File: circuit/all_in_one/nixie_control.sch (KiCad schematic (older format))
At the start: 19 parts

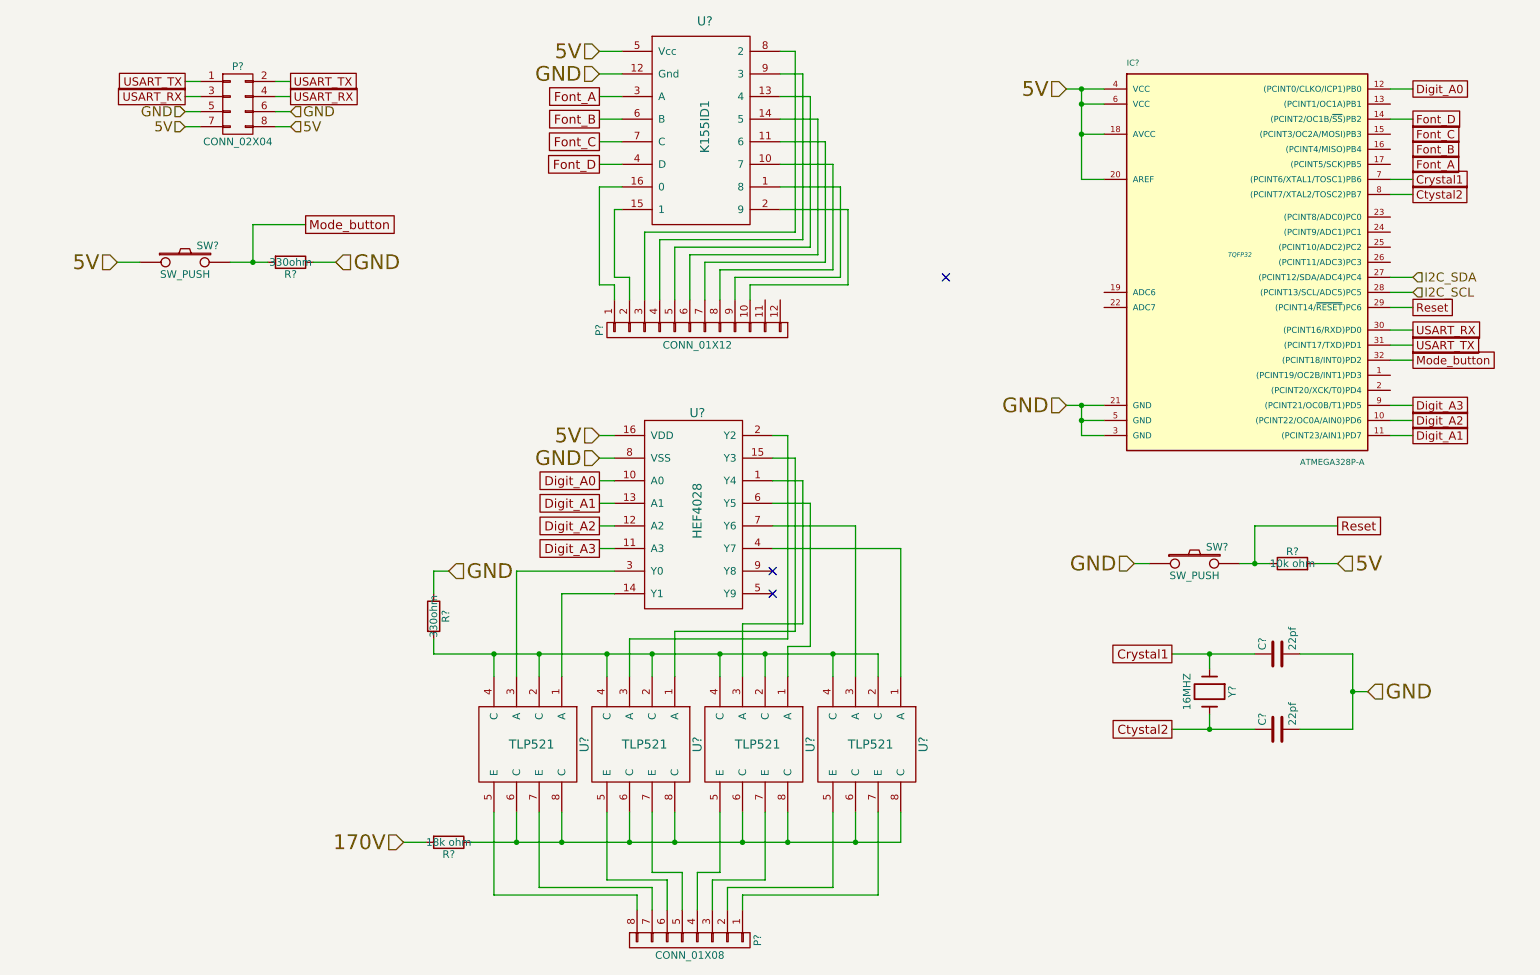
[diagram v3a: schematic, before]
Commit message: [All in one]Define part of compoment's footprint
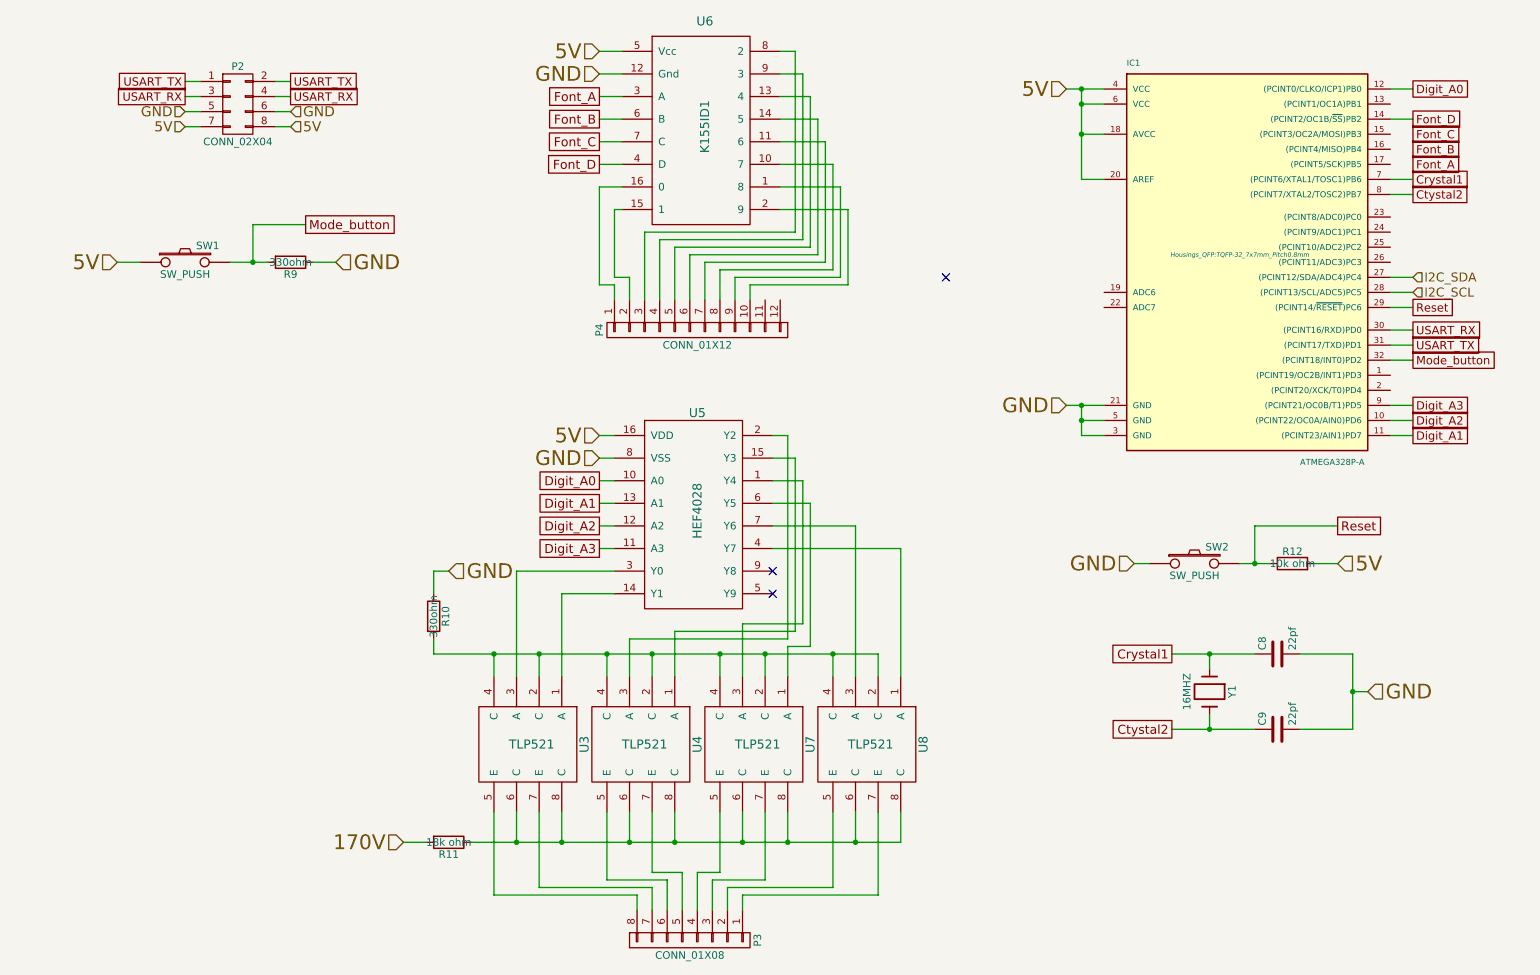
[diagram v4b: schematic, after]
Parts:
- IC1: renamed from IC?; footprint TQFP32 -> Housings_QFP:TQFP-32_7x7mm_Pitch0.8mm
- U3, U4, U7, U8: renamed from U?; footprint (none) -> SMD_Packages:DIP-8_SMD
- U5: renamed from U?; footprint (none) -> SMD_Packages:SO-16-N
- U6: renamed from U?; footprint (none) -> Housings_DIP:DIP-16_W7.62mm
- Y1: renamed from Y?; footprint (none) -> Crystals:Crystal_HC49-U_Vertical
- gave numbers to parts that had none: 11
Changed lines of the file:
@@
 GND
 $Comp
-L ATMEGA328P-A IC?
+L ATMEGA328P-A IC1
 U 1 1 5646C06F
 P 8850 2550
-F 0 "IC?" H 8100 3800 40  0000 L BNN
+F 0 "IC1" H 8100 3800 40  0000 L BNN
 F 1 "ATMEGA328P-A" H 9250 1150 40  0000 L BNN
-F 2 "TQFP32" H 8850 2550 30  0000 C CIN
+F 2 "Housings_QFP:TQFP-32_7x7mm_Pitch0.8mm" H 8850 2550 30  0000 C CIN
 F 3 "" H 8850 2550 60  0000 C CNN
 	1    8850 2550
@@
 5V
 $Comp
-L R R?
+L R R12
 U 1 1 5646C2E9
 P 9200 4600
-F 0 "R?" V 9280 4600 50  0000 C CNN
+F 0 "R12" V 9280 4600 50  0000 C CNN
 F 1 "10k ohm" V 9200 4600 50  0000 C CNN
-F 2 "" V 9130 4600 30  0000 C CNN
+F 2 "" V 9130 4600 30  0001 C CNN
 F 3 "" H 9200 4600 30  0000 C CNN
 	1    9200 4600
@@
 $EndComp
 $Comp
-L SW_PUSH SW?
+L SW_PUSH SW2
 U 1 1 5646C38C
 P 8550 4600
-F 0 "SW?" H 8700 4710 50  0000 C CNN
+F 0 "SW2" H 8700 4710 50  0000 C CNN
 F 1 "SW_PUSH" H 8550 4520 50  0000 C CNN
-F 2 "" H 8550 4600 60  0000 C CNN
+F 2 "" H 8550 4600 60  0001 C CNN
 F 3 "" H 8550 4600 60  0000 C CNN
 	1    8550 4600
@@
 Reset
 $Comp
-L C C?
+L C C8
 U 1 1 5646C6D0
 P 9100 5200
-F 0 "C?" H 9125 5300 50  0000 L CNN
+F 0 "C8" H 9125 5300 50  0000 L CNN
 F 1 "22pf" H 9125 5100 50  0000 L CNN
-F 2 "" H 9138 5050 30  0000 C CNN
+F 2 "" H 9138 5050 30  0001 C CNN
 F 3 "" H 9100 5200 60  0000 C CNN
 	1    9100 5200
@@
 $EndComp
 $Comp
-L C C?
+L C C9
 U 1 1 5646C741
 P 9100 5700
-F 0 "C?" H 9125 5800 50  0000 L CNN
+F 0 "C9" H 9125 5800 50  0000 L CNN
 F 1 "22pf" H 9125 5600 50  0000 L CNN
-F 2 "" H 9138 5550 30  0000 C CNN
+F 2 "" H 9138 5550 30  0001 C CNN
 F 3 "" H 9100 5700 60  0000 C CNN
 	1    9100 5700
@@
 $EndComp
 $Comp
-L Crystal Y?
+L Crystal Y1
 U 1 1 5646C7E1
 P 8650 5450
-F 0 "Y?" H 8650 5600 50  0000 C CNN
+F 0 "Y1" H 8650 5600 50  0000 C CNN
 F 1 "16MHZ" H 8650 5300 50  0000 C CNN
-F 2 "" H 8650 5450 60  0000 C CNN
+F 2 "Crystals:Crystal_HC49-U_Vertical" H 8650 5450 60  0001 C CNN
 F 3 "" H 8650 5450 60  0000 C CNN
 	1    8650 5450
@@
 Ctystal2
 $Comp
-L K155ID1 U?
+L K155ID1 U6
 U 1 1 5646D245
 P 5300 1750
-F 0 "U?" H 5300 2500 60  0000 C CNN
+F 0 "U6" H 5300 2500 60  0000 C CNN
 F 1 "K155ID1" V 5300 1800 60  0000 C CNN
-F 2 "" H 5300 2500 60  0000 C CNN
+F 2 "Housings_DIP:DIP-16_W7.62mm" H 5300 2500 60  0001 C CNN
 F 3 "" H 5300 2500 60  0000 C CNN
 	1    5300 1750
@@
 $EndComp
 $Comp
-L HEF4028 U?
+L HEF4028 U5
 U 1 1 5646D789
 P 5250 4300
-F 0 "U?" H 5250 5000 60  0000 C CNN
+F 0 "U5" H 5250 5000 60  0000 C CNN
 F 1 "HEF4028" V 5250 4350 60  0000 C CNN
-F 2 "" H 5250 5000 60  0000 C CNN
+F 2 "SMD_Packages:SO-16-N" H 5250 5000 60  0001 C CNN
 F 3 "" H 5250 5000 60  0000 C CNN
 	1    5250 4300
@@
 $EndComp
 $Comp
-L TLP521 U?
+L TLP521 U4
 U 1 1 5646D9AA
 P 4850 5800
-F 0 "U?" H 4850 6200 60  0000 C CNN
+F 0 "U4" H 4850 6200 60  0000 C CNN
 F 1 "TLP521" V 4850 5850 60  0000 C CNN
-F 2 "" H 4850 6200 60  0000 C CNN
+F 2 "SMD_Packages:DIP-8_SMD" H 4850 6200 60  0001 C CNN
 F 3 "" H 4850 6200 60  0000 C CNN
 	1    4850 5800
@@
 $EndComp
 $Comp
-L TLP521 U?
+L TLP521 U3
 U 1 1 5646DC40
 P 4100 5800
-F 0 "U?" H 4100 6200 60  0000 C CNN
+F 0 "U3" H 4100 6200 60  0000 C CNN
 F 1 "TLP521" V 4100 5850 60  0000 C CNN
-F 2 "" H 4100 6200 60  0000 C CNN
+F 2 "SMD_Packages:DIP-8_SMD" H 4100 6200 60  0001 C CNN
 F 3 "" H 4100 6200 60  0000 C CNN
 	1    4100 5800
@@
 $EndComp
 $Comp
-L TLP521 U?
+L TLP521 U8
 U 1 1 5646DD0A
 P 6350 5800
-F 0 "U?" H 6350 6200 60  0000 C CNN
+F 0 "U8" H 6350 6200 60  0000 C CNN
 F 1 "TLP521" V 6350 5850 60  0000 C CNN
-F 2 "" H 6350 6200 60  0000 C CNN
+F 2 "SMD_Packages:DIP-8_SMD" H 6350 6200 60  0001 C CNN
 F 3 "" H 6350 6200 60  0000 C CNN
 	1    6350 5800
@@
 $EndComp
 $Comp
-L TLP521 U?
+L TLP521 U7
 U 1 1 5646DD10
 P 5600 5800
-F 0 "U?" H 5600 6200 60  0000 C CNN
+F 0 "U7" H 5600 6200 60  0000 C CNN
 F 1 "TLP521" V 5600 5850 60  0000 C CNN
-F 2 "" H 5600 6200 60  0000 C CNN
+F 2 "SMD_Packages:DIP-8_SMD" H 5600 6200 60  0001 C CNN
 F 3 "" H 5600 6200 60  0000 C CNN
 	1    5600 5800
@@
 Digit_A3
 $Comp
-L R R?
+L R R11
 U 1 1 564700B5
 P 3600 6450
-F 0 "R?" V 3680 6450 50  0000 C CNN
+F 0 "R11" V 3680 6450 50  0000 C CNN
 F 1 "18k ohm" V 3600 6450 50  0000 C CNN
-F 2 "" V 3530 6450 30  0000 C CNN
+F 2 "" V 3530 6450 30  0001 C CNN
 F 3 "" H 3600 6450 30  0000 C CNN
 	1    3600 6450
@@
 $EndComp
 $Comp
-L CONN_01X08 P?
+L CONN_01X08 P3
 U 1 1 564704DB
 P 5200 7100
-F 0 "P?" H 5200 7550 50  0000 C CNN
+F 0 "P3" H 5200 7550 50  0000 C CNN
 F 1 "CONN_01X08" V 5300 7100 50  0000 C CNN
-F 2 "" H 5200 7100 60  0000 C CNN
+F 2 "" H 5200 7100 60  0001 C CNN
 F 3 "" H 5200 7100 60  0000 C CNN
 	1    5200 7100
@@
 Font_D
 $Comp
-L CONN_01X12 P?
+L CONN_01X12 P4
 U 1 1 56472490
 P 5250 3050
-F 0 "P?" H 5250 3700 50  0000 C CNN
+F 0 "P4" H 5250 3700 50  0000 C CNN
 F 1 "CONN_01X12" V 5350 3050 50  0000 C CNN
-F 2 "" H 5250 3050 60  0000 C CNN
+F 2 "" H 5250 3050 60  0001 C CNN
 F 3 "" H 5250 3050 60  0000 C CNN
 	1    5250 3050
@@
 	9850 3150 10000 3150
 $Comp
-L CONN_02X04 P?
+L CONN_02X04 P2
 U 1 1 56476352
 P 2200 1550
-F 0 "P?" H 2200 1800 50  0000 C CNN
+F 0 "P2" H 2200 1800 50  0000 C CNN
 F 1 "CONN_02X04" H 2200 1300 50  0000 C CNN
-F 2 "" H 2200 350 60  0000 C CNN
+F 2 "" H 2200 350 60  0001 C CNN
 F 3 "" H 2200 350 60  0000 C CNN
 	1    2200 1550
@@
 5V
 $Comp
-L SW_PUSH SW?
+L SW_PUSH SW1
 U 1 1 56478717
 P 1850 2600
-F 0 "SW?" H 2000 2710 50  0000 C CNN
+F 0 "SW1" H 2000 2710 50  0000 C CNN
 F 1 "SW_PUSH" H 1850 2520 50  0000 C CNN
-F 2 "" H 1850 2600 60  0000 C CNN
+F 2 "" H 1850 2600 60  0001 C CNN
 F 3 "" H 1850 2600 60  0000 C CNN
 	1    1850 2600
@@
 $EndComp
 $Comp
-L R R?
+L R R9
 U 1 1 5647877C
 P 2550 2600
-F 0 "R?" V 2630 2600 50  0000 C CNN
+F 0 "R9" V 2630 2600 50  0000 C CNN
 F 1 "330ohm" V 2550 2600 50  0000 C CNN
-F 2 "" V 2480 2600 30  0000 C CNN
+F 2 "" V 2480 2600 30  0001 C CNN
 F 3 "" H 2550 2600 30  0000 C CNN
 	1    2550 2600
@@
 NoConn ~ 6900 2700
 $Comp
-L R R?
+L R R10
 U 1 1 56483273
 P 3500 4950
-F 0 "R?" V 3580 4950 50  0000 C CNN
+F 0 "R10" V 3580 4950 50  0000 C CNN
 F 1 "330ohm" V 3500 4950 50  0000 C CNN
-F 2 "" V 3430 4950 30  0000 C CNN
+F 2 "" V 3430 4950 30  0001 C CNN
 F 3 "" H 3500 4950 30  0000 C CNN
 	1    3500 4950

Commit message: [All in one]Finish the tube display circuit
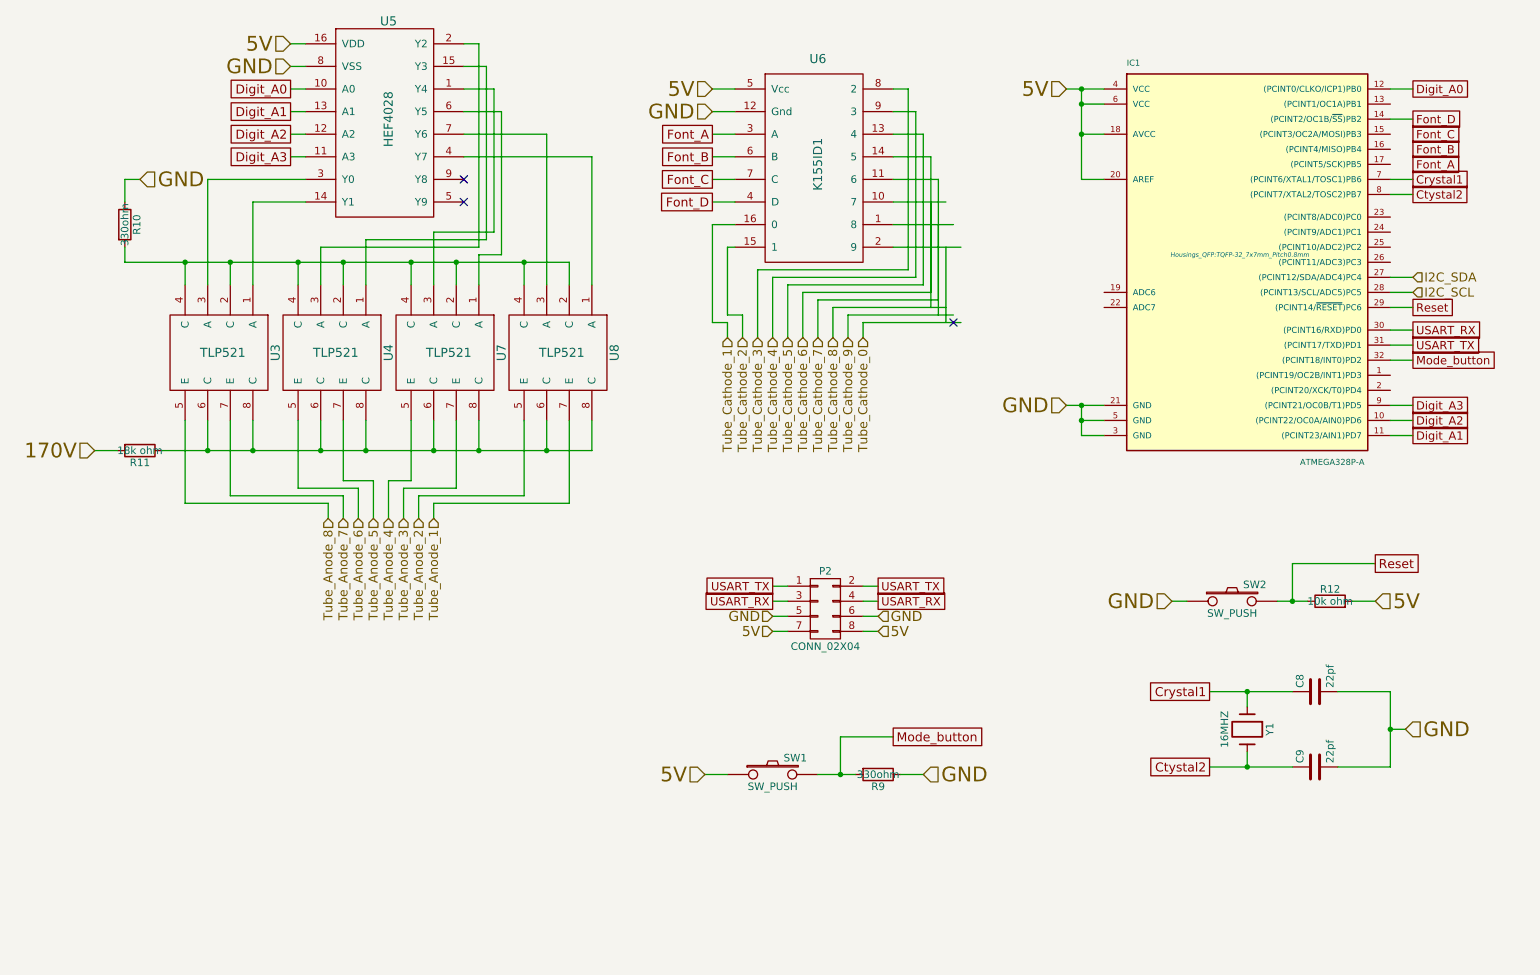
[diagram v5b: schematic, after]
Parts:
- removed P3: CONN_01X08, symbol CONN_01X08
- removed P4: CONN_01X12, symbol CONN_01X12
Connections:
- net labels added: Tube_Anode_1, Tube_Anode_2, Tube_Anode_3, Tube_Anode_4, Tube_Anode_5, Tube_Anode_6, Tube_Anode_7, Tube_Anode_8, Tube_Cathode_0, Tube_Cathode_1, Tube_Cathode_2, Tube_Cathode_3, Tube_Cathode_4, Tube_Cathode_5, Tube_Cathode_6, Tube_Cathode_7, Tube_Cathode_8, Tube_Cathode_9
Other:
- moved on the sheet: C8, C9, P2, R10, R11, R12, R9, SW1, SW2, U3, U4, U5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

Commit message: [All in one]Add tube comma control circuit
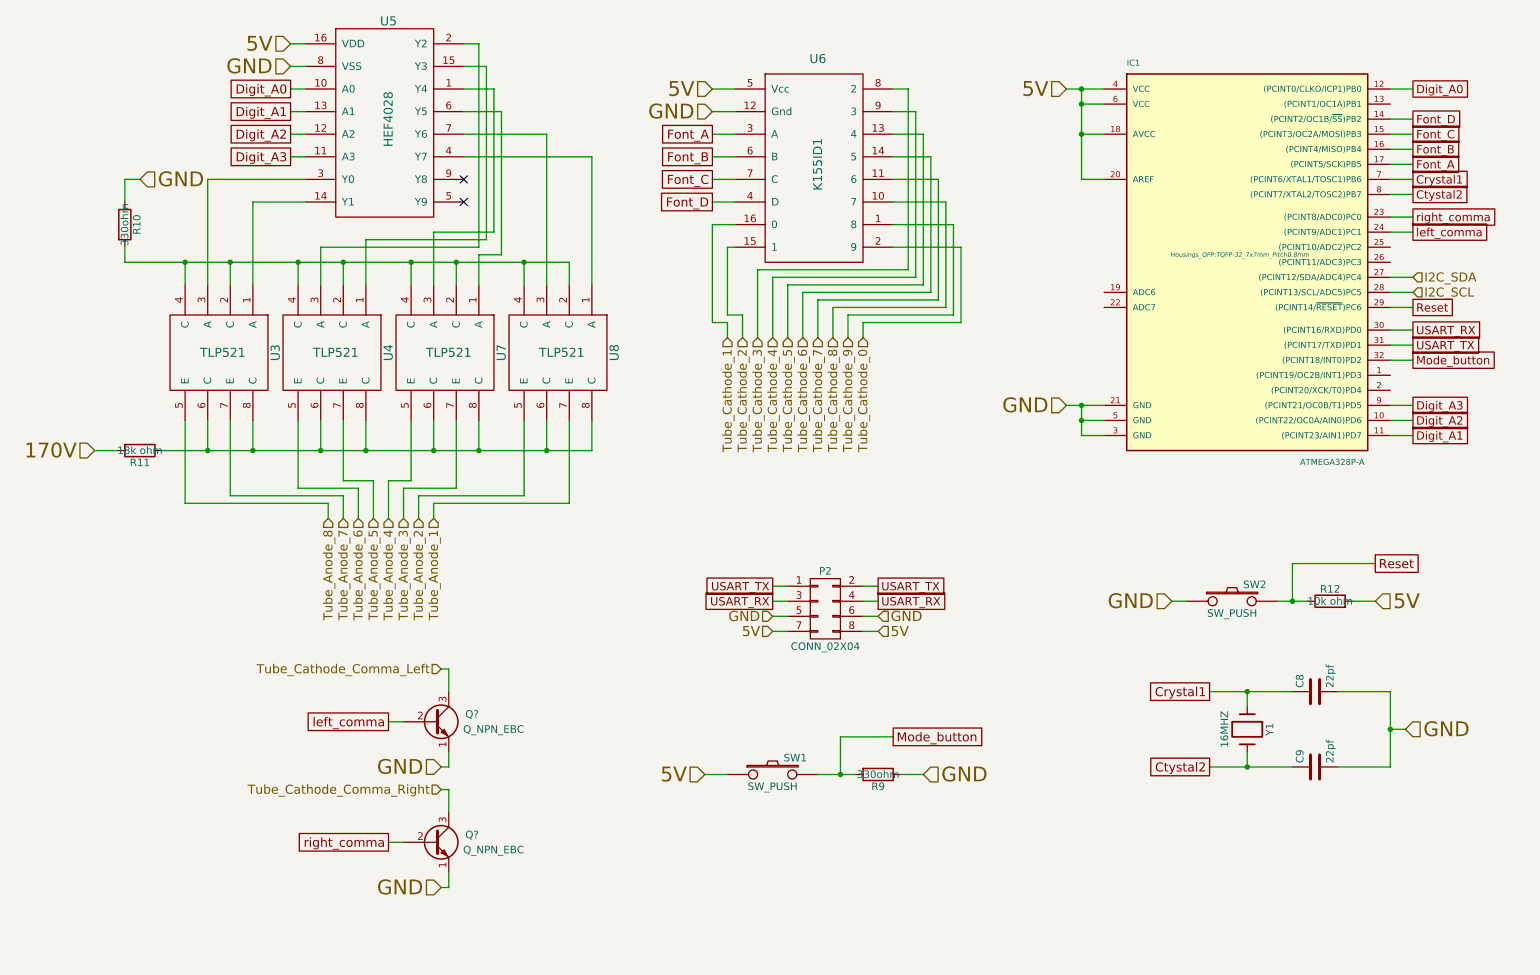
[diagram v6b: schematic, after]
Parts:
- added Q? (x2): Q_NPN_EBC, symbol Q_NPN_EBC
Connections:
- net labels added: Tube_Cathode_Comma_Left, Tube_Cathode_Comma_Right, left_comma, right_comma
- wire segments 170 -> 185
- no-connect marks 3 -> 2
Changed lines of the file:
@@
 	6550 2200 6900 2200
 Wire Wire Line
-	6800 2200 6800 2900
+	6900 2200 6900 2900
 Wire Wire Line
 	6900 2900 6150 2900
@@
 	6550 2350 6950 2350
 Wire Wire Line
-	6850 2350 6850 2950
+	6950 2350 6950 2950
 Wire Wire Line
 	6950 2950 6250 2950
@@
 	6350 3000 7000 3000
 Wire Wire Line
-	6900 3000 6900 2500
+	7000 3000 7000 2500
 Wire Wire Line
 	7000 2500 6550 2500
@@
 	6200 5750 6550 5750
 Connection ~ 6200 6000
-NoConn ~ 6950 3000
 $Comp
 L R R10
@@
 Text HLabel 6350 3100 3    60   Input ~ 0
 Tube_Cathode_0
+$Comp
+L Q_NPN_EBC Q?
+U 1 1 56531503
+P 3500 5650
+F 0 "Q?" H 3800 5700 50  0000 R CNN
+F 1 "Q_NPN_EBC" H 4100 5600 50  0000 R CNN
+F 2 "" H 3700 5750 29  0000 C CNN
+F 3 "" H 3500 5650 60  0000 C CNN
+	1    3500 5650
+	1    0    0    -1
+$EndComp
+$Comp
+L Q_NPN_EBC Q?
+U 1 1 56531680
+P 3500 6450
+F 0 "Q?" H 3800 6500 50  0000 R CNN
+F 1 "Q_NPN_EBC" H 4100 6400 50  0000 R CNN
+F 2 "" H 3700 6550 29  0000 C CNN
+F 3 "" H 3500 6450 60  0000 C CNN
+	1    3500 6450
+	1    0    0    -1
+$EndComp
+Text HLabel 3550 5300 0    60   Input ~ 0
+Tube_Cathode_Comma_Left
+Text HLabel 3550 6100 0    60   Input ~ 0
+Tube_Cathode_Comma_Right
+Wire Wire Line
+	3550 5300 3600 5300
+Wire Wire Line
+	3600 5300 3600 5450
+Wire Wire Line
+	3550 6100 3600 6100
+Wire Wire Line
+	3600 6100 3600 6250
+Text HLabel 3550 5950 0    98   Input ~ 0
+GND
+Text HLabel 3550 6750 0    98   Input ~ 0
+GND
+Wire Wire Line
+	3550 5950 3600 5950
+Wire Wire Line
+	3600 5950 3600 5850
+Wire Wire Line
+	3550 6750 3600 6750
+Wire Wire Line
+	3600 6750 3600 6650
+Text GLabel 3200 6450 0    60   UnSpc ~ 0
+right_comma
+Text GLabel 3200 5650 0    60   UnSpc ~ 0
+left_comma
+Wire Wire Line
+	3200 5650 3300 5650
+Wire Wire Line
+	3200 6450 3300 6450
+Text GLabel 10000 2300 2    55   UnSpc ~ 0
+right_comma
+Text GLabel 10000 2400 2    55   UnSpc ~ 0
+left_comma
+Wire Wire Line
+	9850 2300 10000 2300
+Wire Wire Line
+	9850 2400 10000 2400
+Wire Wire Line
+	9850 1750 10000 1750
+Wire Wire Line
+	9850 1850 10000 1850
+Wire Wire Line
+	9850 1950 10000 1950
 $EndSCHEMATC
